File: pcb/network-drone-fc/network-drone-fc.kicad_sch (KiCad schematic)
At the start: 85 parts, among them J1 U.FL-R-SMT-1, J2 TYPE-C 16PIN 2MD, J3 U.FL GPS, J4 ESC, J5 Sensor port 5V I2C, J6 Radio UART 5V, J7 Charging board, J8 Landing sensor 5V I2C, U1 ESP32-S3FN8, U2 USBLC6-2SC6, U3 AP63205WU-7, U4 TLV75733PDRVR, U5 TPS7A2033PDBVR, U6 ICM-42688-P, U7 BMP581, U8 MAX-M10S, X1 FA-128 40MHz 10pF

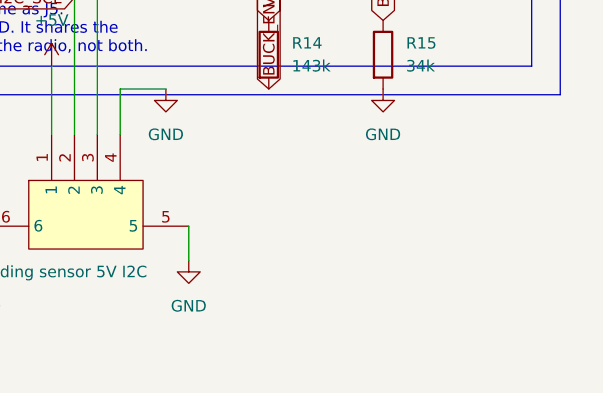
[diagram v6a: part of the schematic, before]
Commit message: ESP32 supply capacitors at the pins' plane vias
C37 (1 uF) on the VDDA pins 55 and 56, C38 (0.1 uF) on VDD3P3_CPU and
C39 (0.1 uF) on VDD3P3_RTC, all on the bottom directly under each pin's
via. The nearest capacitors before were 4 to 7 mm away.
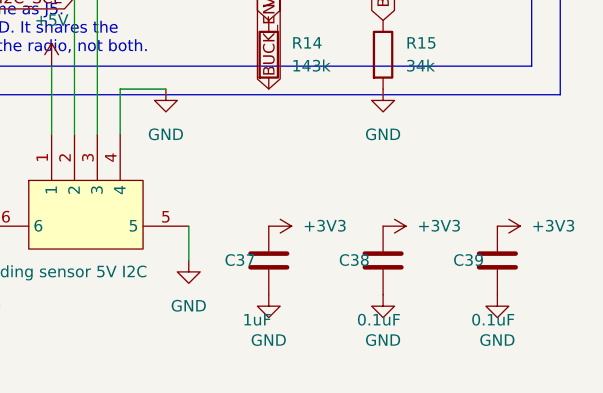
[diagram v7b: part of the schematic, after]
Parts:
- added C37: 1uF, Capacitor_SMD:C_0402_1005Metric, symbol Device:C
- added C38, C39: 0.1uF, Capacitor_SMD:C_0402_1005Metric, symbol Device:C
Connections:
- net +3V3: now also C37.1, C38.1, C39.1
- net GND: now also C37.2, C38.2, C39.2

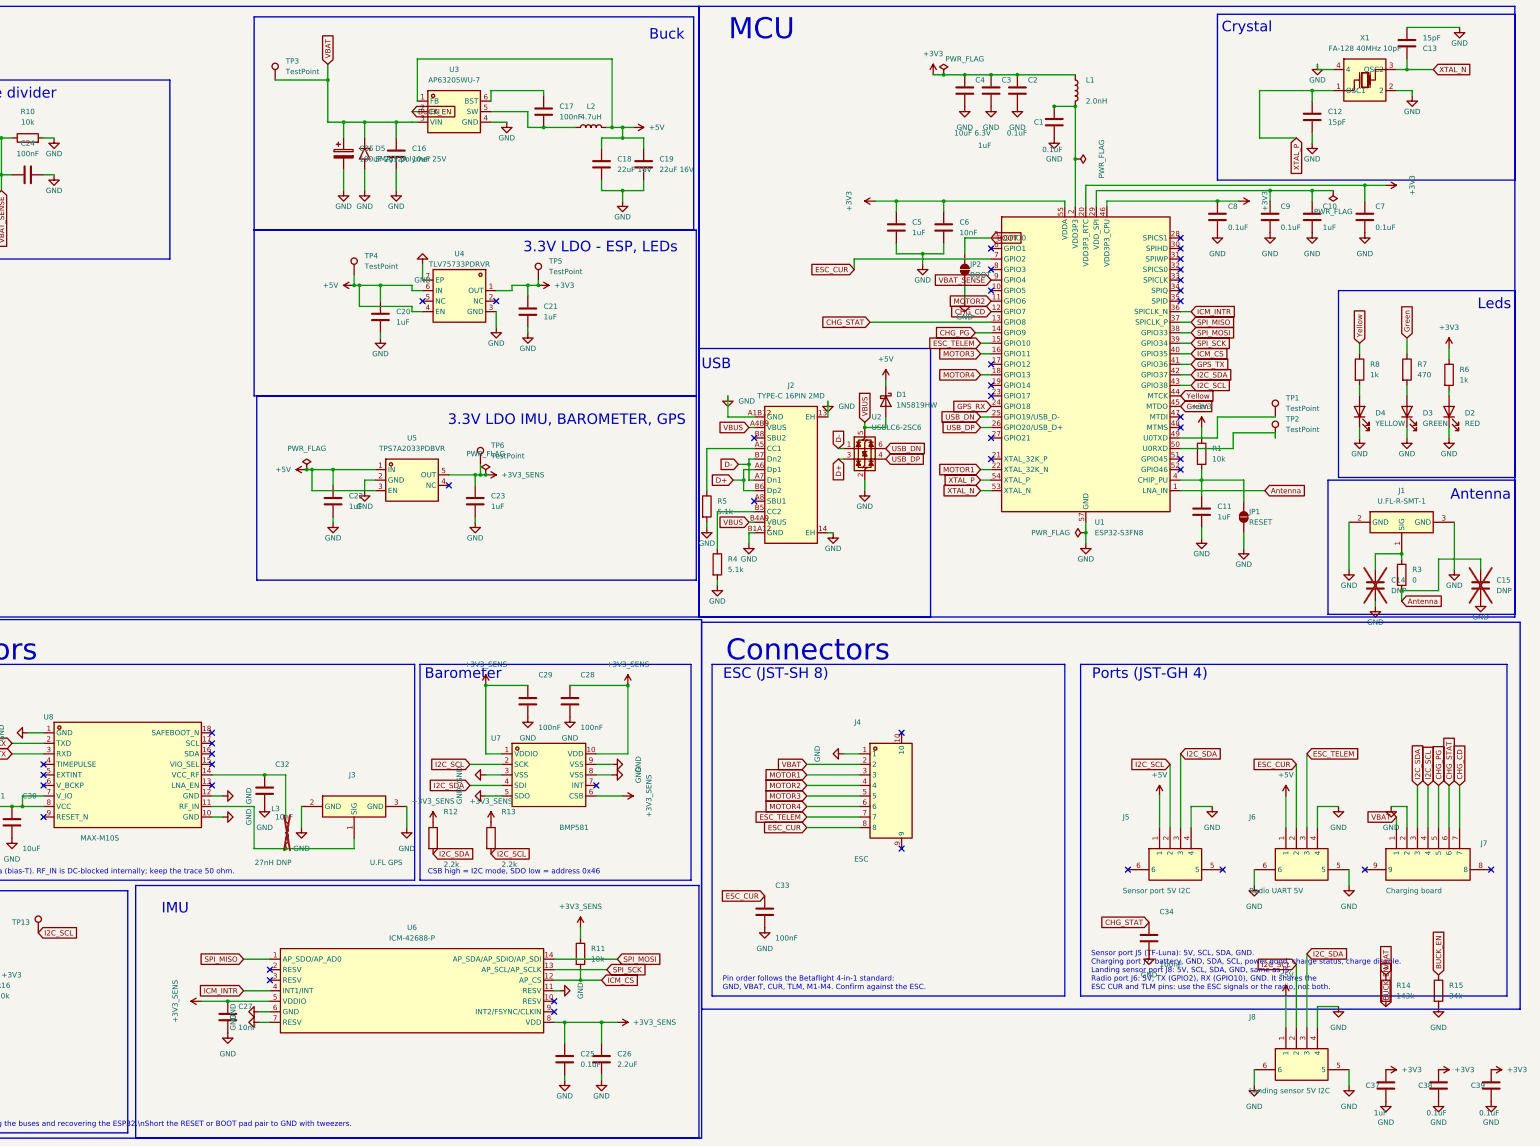
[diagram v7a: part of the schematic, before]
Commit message: 24 nH series inductor on the crystal's XTAL_P line
Espressif's hardware design guide asks for a series part on XTAL_P,
starting at 24 nH, to keep the crystal's harmonics out of the radio. L4
sits in the existing vertical run beside the crystal. The chip side of
the line is now the net XTAL_P_CHIP.

The schematic symbols for R14, R15 and C37 to C39 also move out of the
title block and a text note into empty space, with their labels drawn
the right way round.
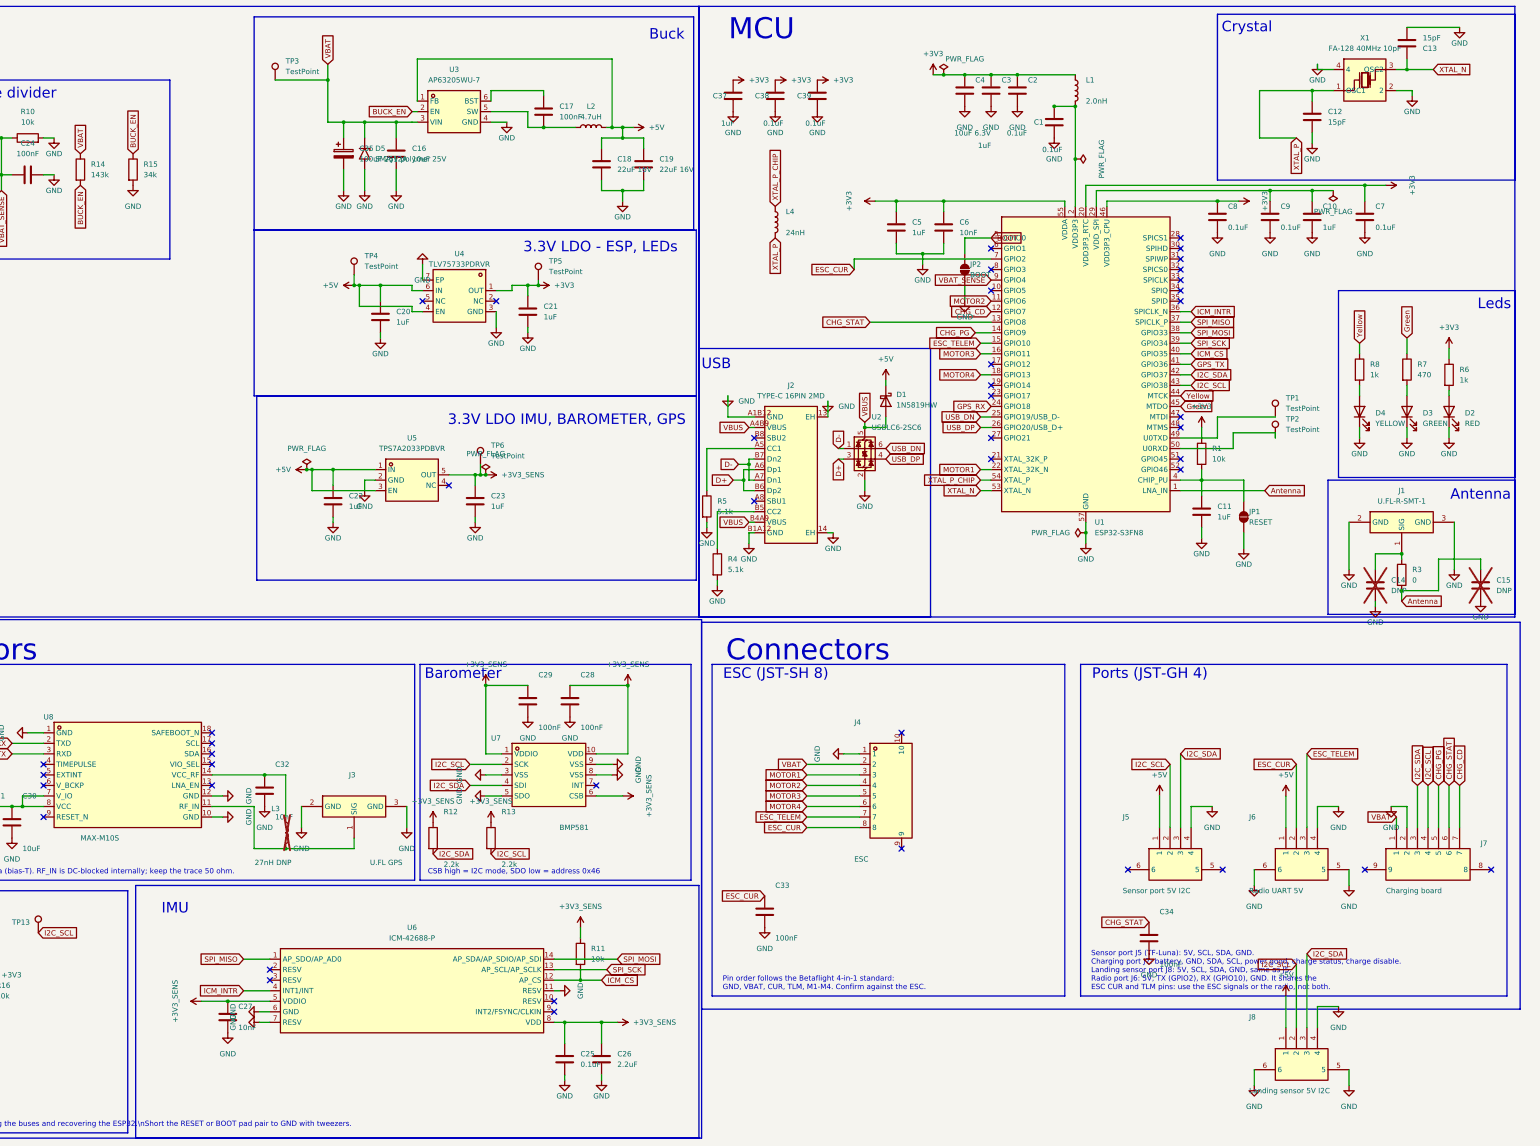
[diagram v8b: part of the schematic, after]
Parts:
- added L4: 24nH, Inductor_SMD:L_0402_1005Metric, symbol Device:L
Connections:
- net XTAL_P: now also L4.2; no longer U1.54 (XTAL_P)
- new net XTAL_P_CHIP: L4.1, U1.54 (XTAL_P)
